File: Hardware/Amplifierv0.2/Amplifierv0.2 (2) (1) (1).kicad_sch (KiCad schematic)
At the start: 62 parts, among them IC1 BQ25306RTET, J1 Conn_01x03, J2 Conn_01x03, Q1 SI2304DDS-T1-GE3, U1 SI2303CDS-T1-GE3, U2 LM78L05_SO8

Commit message: Ampli v6
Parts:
- removed CR?: ESDA25P35-1U1M, QFN1610_STM, symbol ESDA25P35-1U1M:ESDA25P35-1U1M
- removed D?: LED, symbol Device:LED
- removed IC1: BQ25306RTET, WQFN16_3X3_TEX, symbol BQ25306:BQ25306RTET
- removed U2: LM78L05_SO8, Package_SO:SOIC-8_3.9x4.9mm_P1.27mm, symbol Regulator_Linear:LM78L05_SO8
- removed U?: UCC37325D, D8, symbol UCC37325D:UCC37325D
- removed U?: LM1117DT-3.3, Package_TO_SOT_SMD:TO-252-3_TabPin2, symbol Regulator_Linear:LM1117DT-3.3
- added BQ25306RTET1: ~, Package_DFN_QFN:WQFN-16-1EP_3x3mm_P0.5mm_EP1.75x1.75mm, symbol BQ25306RTET:BQ25306RTET
- added BU18SD5WG-TR1, BU33SD5WG-TR1, BU33SD5WG-TR2: LM1117DT-3.3, Package_TO_SOT_SMD:SOT-23-5, symbol Regulator_Linear:MCP1802x-xx02xOT
- added C16, C17, C18: 1u, Capacitor_SMD:C_0603_1608Metric_Pad1.08x0.95mm_HandSolder, symbol Device:C_Small
- added D2: LED_Small, LED_SMD:LED_0603_1608Metric_Pad1.05x0.95mm_HandSolder, symbol Device:LED_Small
- added D3: D_Schottky, symbol Device:D_Schottky
- added L2: 39n, Inductor_SMD:L_0805_2012Metric_Pad1.05x1.20mm_HandSolder, symbol Device:L_Small
- added U8: AZ1117-5.0, Package_TO_SOT_SMD:SOT-223-3_TabPin2, symbol Regulator_Linear:AZ1117-5.0
- added UCC27325DR1: ~, Package_SO:SOIC-8-N7_3.9x4.9mm_P1.27mm, symbol UCC27325DR:UCC27325DR
- C1: value 0.33uF -> 10uF; footprint (none) -> Capacitor_SMD:C_0603_1608Metric_Pad1.08x0.95mm_HandSolder
- C10: value 0.1 -> 1u; footprint (none) -> Capacitor_SMD:C_0603_1608Metric_Pad1.08x0.95mm_HandSolder
- C11, C12, C14, C15, C2, C4, C6: renamed from C?; footprint (none) -> Capacitor_SMD:C_0603_1608Metric_Pad1.08x0.95mm_HandSolder
- C21, C22, C5, C7: footprint (none) -> Capacitor_SMD:C_0603_1608Metric_Pad1.08x0.95mm_HandSolder
- C3: value 0.1uF -> 22uF; footprint (none) -> Capacitor_SMD:C_0603_1608Metric_Pad1.08x0.95mm_HandSolder
- C8: value 10u -> 1u; footprint (none) -> Capacitor_SMD:C_0603_1608Metric_Pad1.08x0.95mm_HandSolder
- C9: value 22u -> 1u; footprint (none) -> Capacitor_SMD:C_0603_1608Metric_Pad1.08x0.95mm_HandSolder
- J1, J2: footprint (none) -> Connector_JST:JST_XH_B3B-XH-A_1x03_P2.50mm_Vertical
- L1: value 6R8 -> ??????????????; footprint (none) -> Inductor_SMD:L_0805_2012Metric_Pad1.05x1.20mm_HandSolder
- Q1: footprint SOT-23_SI2304_VIS -> Package_TO_SOT_SMD:SOT-23
- Q2: renamed from Q?; footprint SOT-23_SI2304_VIS -> Package_TO_SOT_SMD:SOT-23
- R1, R10, R11, R12, R13, R14, R15, R16, R2, R3, R8, R9: renamed from R?; footprint (none) -> Resistor_SMD:R_0603_1608Metric_Pad0.98x0.95mm_HandSolder
- R31, R32, R4, R5, R6, R7: footprint (none) -> Resistor_SMD:R_0603_1608Metric_Pad0.98x0.95mm_HandSolder
- RV10k1: renamed from RV10k; footprint (none) -> Resistor_SMD:R_0603_1608Metric_Pad0.98x0.95mm_HandSolder
- U1: footprint TO-236_VIS -> Package_TO_SOT_SMD:SOT-23
- U3: renamed from U?; footprint TO-236_VIS -> Package_TO_SOT_SMD:SOT-23
- U4: renamed from U?; value STM32G491CETx -> STM32G491CETx (x=6)
- gave numbers to parts that had none: 7
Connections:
- net 3.3V: now also BU18SD5WG-TR1.1 (VIN), BU18SD5WG-TR1.3 (~{SHDN}), C16.1; no longer C10.1, C9.1
- net 5V: now also C10.1, C21.2, C22.2, BU33SD5WG-TR1.1 (VIN), BU33SD5WG-TR1.3 (~{SHDN}), L2.1, U8.2 (VO), UCC27325DR1.6 (VDD)
- net GND: now also BQ25306RTET1.11 (GND), BQ25306RTET1.12 (GND), BQ25306RTET1.17 (TP), BU18SD5WG-TR1.2 (GND), BU33SD5WG-TR1.2 (GND), BU33SD5WG-TR2.2 (GND), C16.2, C17.2, C18.2, U8.1 (GND); no longer IC1.10 (DB/), IC1.11 (FLT/), IC1.12 (VCC)
- net REGN: now also BQ25306RTET1.2 (REGN), D2.2 (A)
- net UCPD_CC2: now also U4.41 (PB4), D3.1 (K)
- net VBUS (9V): now also BQ25306RTET1.1 (VBUS)
- net V_BAT+: now also BQ25306RTET1.10 (BAT); no longer C8.1
- net V_BAT-: now also BQ25306RTET1.7 (TS)
- net V_HO: now also UCC27325DR1.7 (OUTA)
- net V_LO: now also UCC27325DR1.5 (OUTB)
- net V_SYS: now also BQ25306RTET1.16 (PMID), U8.3 (VI)
- net at R10.1: now also BQ25306RTET1.3 (STAT)
- net at R10.2: now also D2.1 (K)
- net LIGHT: now reaches U4.12 (PA4)
- net TIM3_CH1: now reaches U4.14 (PA6)
- net TIM3_CH2: now reaches U4.15 (PA7)
- net A Encodeur 1: now reaches U4.2 (PC13)
- net Potar_volume: now reaches U4.28 (PB14)
- net B Encodeur 1: now reaches U4.3 (PC14)
- net I2S_SCLK: now reaches U4.30 (PA8)
- net I2S_SCLK: now also U6.15 (I2S_SCLK)
- net I2S_LRCLK: now reaches U4.31 (PA9)
- net I2S_LRCLK: now also U6.14 (I2S_LRCLK)
- net I2S_DIN: now reaches U4.32 (PA10)
- net I2S_DIN: now also U6.17 (I2S_DIN)
- net USB_DM: now reaches U4.33 (PA11)
- net USB_DP: now reaches U4.34 (PA12)
- net I2S_DOUT: now reaches U4.37 (PA13)
- net I2S_DOUT: now also U6.16 (I2S_DOUT)
- net CTRL_DATA: now reaches U4.38 (PA14)
- net CTRL_DATA: now also U6.18 (CTRL_DATA)
- net USART_RX: now reaches U4.39 (PA15)
- net A Encodeur 2: now reaches U4.4 (PC15)
- net USART2_TX: now reaches U4.40 (PB3)
- net UCPD1_CC1: now reaches U4.43 (PB6)
- net CTRL_CLK: now reaches U4.45 (PB8)
- net CTRL_CLK: now also U6.19 (CTRL_CLK)
- net B Encodeur 2: now reaches U4.5 (PF0)
- net at C13.2, R31.2: now also R32.2, BQ25306RTET1.9 (FB); no longer R32.1
- net at R11.1: now also BQ25306RTET1.4 (ICHG)
- net at C14.2, L2.1: now also BQ25306RTET1.13 (SW), BQ25306RTET1.14 (SW)
- net at C21.1, C22.1: now also UCC27325DR1.3 (GND)
- net at D1.1 (K), J3.A4 (VBUS), J3.A9 (VBUS)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: now also D3.2 (A)
- net at C14.1: now also BQ25306RTET1.15 (BTST)
- net V_ADC_potar1 renamed OUT_L
- net V_ADC_potar2 renamed OUT_R
- net V_ADC_potar3: no longer names the net of U4.10 (PA2)
- net V_ADC_potar4 renamed SYS_MCLK
- net V_ADC_potar5 renamed TIM3_CH3
- net V_ADC_potar6 renamed TIM3_CH4
- net V_ADC_potar7 renamed EQ_BAND_BTN
- new net: BU33SD5WG-TR2.1 (VIN), BU33SD5WG-TR2.3 (~{SHDN}), C8.1, L2.2
- new net: BQ25306RTET1.8 (FB_GND), R32.1
- new net 1.8V: BU18SD5WG-TR1.5 (VOUT), C18.1
- new net 3.3VAC: BU33SD5WG-TR2.5 (VOUT), C9.1
- new net 3.3VDC: BU33SD5WG-TR1.5 (VOUT), C17.1
- new net GPIO_01: IC1.12 (VCC)
- new net GPIO_02: IC1.10 (DB/)
- new net GPIO_03: IC1.11 (FLT/)
- no-connect marks 18 -> 13
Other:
- note added: "A connecter au codec"
- note added: "Alternatif"
- note added: "Check Mosfet"
- note added: "Continu"
- note removed: "A trouver les bons pins :"
- note removed: "BAT"
- note removed: "BTST"
- note removed: "EN"
- note removed: "FB"
- note removed: "FB_GND"
- note removed: "GND"
- note removed: "ICHG"
- note removed: "PMID"
- note removed: "POL"
- note removed: "REGN"
- note removed: "STAT"
- note removed: "SW"
- note removed: "THERMAL_PAD"
- note removed: "TS"
- note removed: "VBUS"
- moved on the sheet: C1, C11, C12, C13, C14, C15, C2, C3, C4, C6, D1, D4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

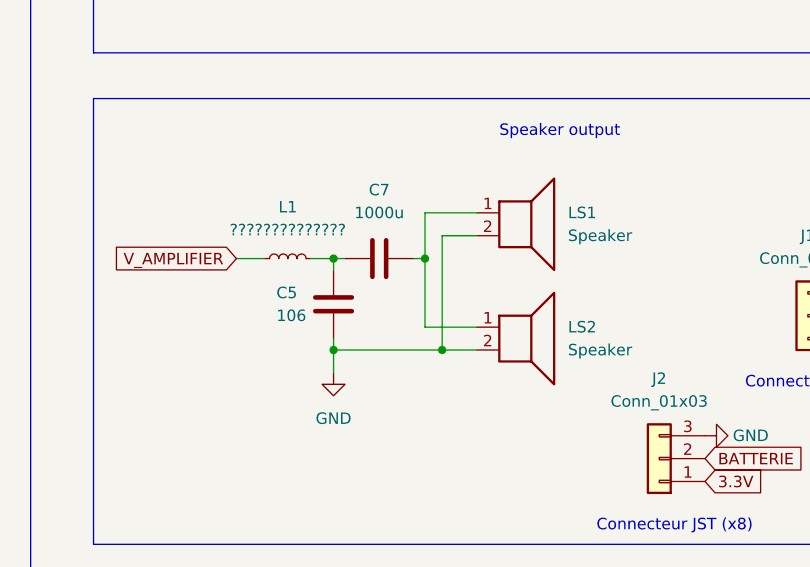
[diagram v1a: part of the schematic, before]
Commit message: mainboard 1.1 in progress
editing capacity values and adding of the STM32 programing connector
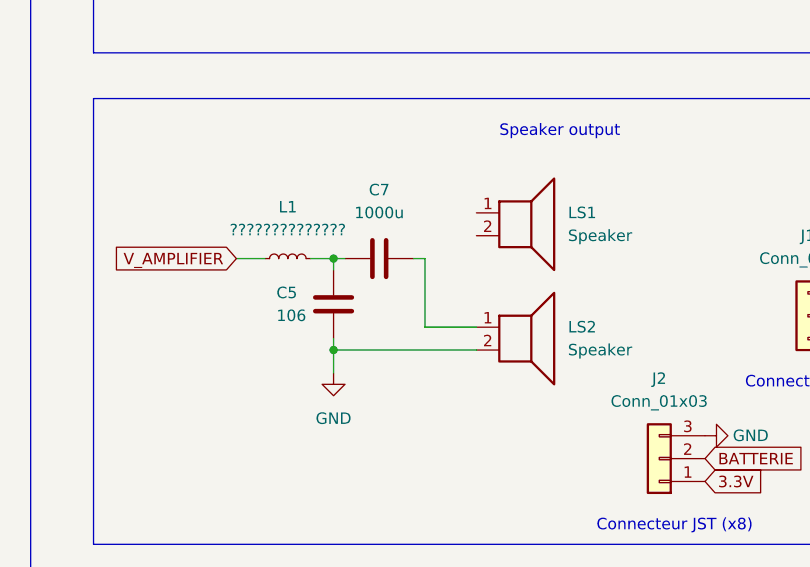
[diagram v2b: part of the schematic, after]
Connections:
- net GND: no longer LS1.2
- net at C7.2, LS2.1: no longer LS1.1
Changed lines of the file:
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@@
   (junction (at 81.28 80.01) (diameter 0) (color 0 0 0 0)
   )
-  (junction (at 339.09 226.695) (diameter 0) (color 0 0 0 0)
-  )
   (junction (at 334.01 128.905) (diameter 0) (color 0 0 0 0)
-  )
-  (junction (at 337.185 216.535) (diameter 0) (color 0 0 0 0)
   )
   (junction (at 364.49 128.905) (diameter 0) (color 0 0 0 0)
@@
     (stroke (width 0) (type default))
   )
-  (wire (pts (xy 342.9 213.995) (xy 339.09 213.995))
-    (stroke (width 0) (type default))
-  )
   (wire (pts (xy 36.195 190.5) (xy 37.465 190.5))
     (stroke (width 0) (type default))
@@
     (stroke (width 0) (type default))
   )
-  (wire (pts (xy 337.185 216.535) (xy 337.185 211.455))
-    (stroke (width 0) (type default))
-  )
-  (wire (pts (xy 339.09 213.995) (xy 339.09 226.695))
-    (stroke (width 0) (type default))
-  )
   (wire (pts (xy 255.905 221.615) (xy 255.905 228.6))
     (stroke (width 0) (type default))
@@
     (stroke (width 0) (type default))
   )
-  (wire (pts (xy 327.025 226.695) (xy 339.09 226.695))
-    (stroke (width 0) (type default))
-  )
   (wire (pts (xy 335.915 216.535) (xy 337.185 216.535))
     (stroke (width 0) (type default))
@@
     (stroke (width 0) (type default))
   )
-  (wire (pts (xy 337.185 211.455) (xy 342.9 211.455))
-    (stroke (width 0) (type default))
-  )
   (wire (pts (xy 390.525 164.465) (xy 397.51 164.465))
     (stroke (width 0) (type default))
@@
     (stroke (width 0) (type default))
   )
-  (wire (pts (xy 339.09 226.695) (xy 342.9 226.695))
-    (stroke (width 0) (type default))
-  )
+  (wire (pts (xy 327.025 226.695) (xy 342.9 226.695))
+    (stroke (width 0) (type default))
+  )
